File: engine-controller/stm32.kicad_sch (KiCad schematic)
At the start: 11 parts, among them IC201 STM32F103RBT6, J201 Conn_ARM_JTAG_SWD_20

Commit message: inital TCs
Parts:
- added C207, C208: 30p, Capacitor_SMD:C_0402_1005Metric, symbol Device:C_Small
- added Y201: 8MHz, Crystal:Crystal_SMD_5032-2Pin_5.0x3.2mm, symbol Device:Crystal_Small
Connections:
- net GND: now also C207.2, C208.2
- net SPI1_NSS: now reaches IC201.20 (PA4)
- net SPI1_SCK: now reaches IC201.21 (PA5)
- net SPI1_MISO: now reaches IC201.22 (PA6)
- net SPI1_MOSI: now reaches IC201.23 (PA7)
- net PC6: now reaches IC201.37 (PC6)
- net PC7: now reaches IC201.38 (PC7)
- net PC8: now reaches IC201.39 (PC8)
- net PC9: now reaches IC201.40 (PC9)
- net PA8: now reaches IC201.41 (PA8)
- net PA9: now reaches IC201.42 (PA9)
- net PA10: now reaches IC201.43 (PA10)
- net PA11: now reaches IC201.44 (PA11)
- net PA12: now reaches IC201.45 (PA12)
- net at IC201.5 (OSC_IN): now also C207.1, Y201.1
- net PB5: now reaches IC201.57 (PB5)
- net PB6: now reaches IC201.58 (PB6)
- net PB7: now reaches IC201.59 (PB7)
- net at IC201.6 (OSC_OUT): now also C208.1, Y201.2
- net PB8: now reaches IC201.61 (PB8)
- net PB9: now reaches IC201.62 (PB9)
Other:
- note added: "CL = 2 * (Cload - Cstray)"

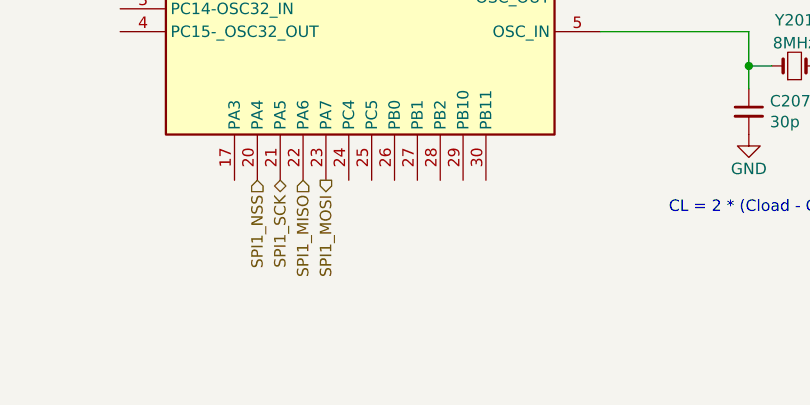
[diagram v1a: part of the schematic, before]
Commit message: added 4-20mA sense circuit
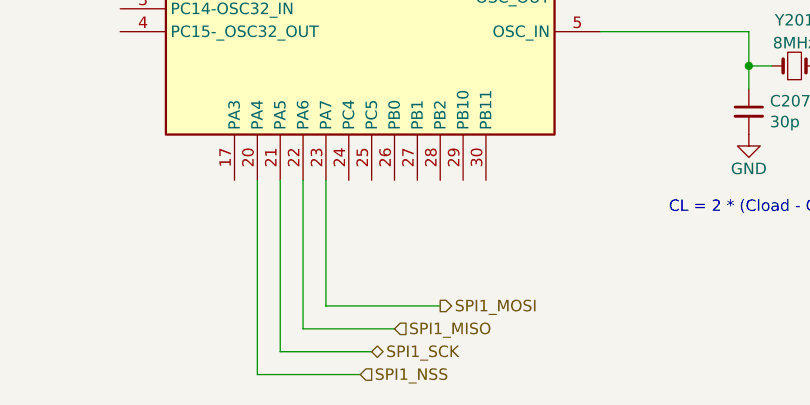
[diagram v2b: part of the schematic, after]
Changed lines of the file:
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@@
   (no_connect (at 71.12 68.58))
   (no_connect (at 71.12 83.82))
+  (wire (pts (xy 199.39 149.86) (xy 199.39 135.89))
+    (stroke (width 0) (type default))
+  )
   (wire (pts (xy 204.47 36.83) (xy 204.47 39.37))
     (stroke (width 0) (type default))
@@
     (stroke (width 0) (type default))
   )
+  (wire (pts (xy 203.2 157.48) (xy 191.77 157.48))
+    (stroke (width 0) (type default))
+  )
+  (wire (pts (xy 194.31 154.94) (xy 194.31 135.89))
+    (stroke (width 0) (type default))
+  )
   (wire (pts (xy 232.41 73.66) (xy 229.87 73.66))
     (stroke (width 0) (type default))
@@
     (stroke (width 0) (type default))
   )
+  (wire (pts (xy 196.85 152.4) (xy 196.85 135.89))
+    (stroke (width 0) (type default))
+  )
   (wire (pts (xy 201.93 33.02) (xy 201.93 39.37))
     (stroke (width 0) (type default))
@@
     (stroke (width 0) (type default))
   )
+  (wire (pts (xy 207.01 152.4) (xy 196.85 152.4))
+    (stroke (width 0) (type default))
+  )
   (wire (pts (xy 148.59 82.55) (xy 148.59 85.09))
     (stroke (width 0) (type default))
@@
     (stroke (width 0) (type default))
   )
+  (wire (pts (xy 204.47 154.94) (xy 194.31 154.94))
+    (stroke (width 0) (type default))
+  )
   (wire (pts (xy 229.87 63.5) (xy 254 63.5))
     (stroke (width 0) (type default))
@@
     (stroke (width 0) (type default))
   )
+  (wire (pts (xy 212.09 149.86) (xy 199.39 149.86))
+    (stroke (width 0) (type default))
+  )
   (wire (pts (xy 246.38 123.19) (xy 248.92 123.19))
     (stroke (width 0) (type default))
@@
   )
   (wire (pts (xy 114.3 53.34) (xy 124.46 53.34))
+    (stroke (width 0) (type default))
+  )
+  (wire (pts (xy 191.77 157.48) (xy 191.77 135.89))
     (stroke (width 0) (type default))
   )
@@
     (effects (font (size 1.27 1.27)) (justify left))
   )
-  (hierarchical_label "SPI1_SCK" (shape bidirectional) (at 194.31 135.89 270) (fields_autoplaced)
-    (effects (font (size 1.27 1.27)) (justify right))
+  (hierarchical_label "SPI1_SCK" (shape bidirectional) (at 204.47 154.94 0) (fields_autoplaced)
+    (effects (font (size 1.27 1.27)) (justify left))
   )
   (hierarchical_label "PC7" (shape output) (at 229.87 93.98 0) (fields_autoplaced)
@@
     (effects (font (size 1.27 1.27)) (justify left))
   )
-  (hierarchical_label "SPI1_MISO" (shape input) (at 196.85 135.89 270) (fields_autoplaced)
-    (effects (font (size 1.27 1.27)) (justify right))
+  (hierarchical_label "SPI1_MISO" (shape input) (at 207.01 152.4 0) (fields_autoplaced)
+    (effects (font (size 1.27 1.27)) (justify left))
   )
   (hierarchical_label "PA8" (shape output) (at 229.87 86.36 0) (fields_autoplaced)
@@
     (effects (font (size 1.27 1.27)) (justify left))
   )
-  (hierarchical_label "SPI1_MOSI" (shape output) (at 199.39 135.89 270) (fields_autoplaced)
-    (effects (font (size 1.27 1.27)) (justify right))
+  (hierarchical_label "SPI1_MOSI" (shape output) (at 212.09 149.86 0) (fields_autoplaced)
+    (effects (font (size 1.27 1.27)) (justify left))
   )
   (hierarchical_label "PB15" (shape output) (at 229.87 99.06 0) (fields_autoplaced)
     (effects (font (size 1.27 1.27)) (justify left))
   )
-  (hierarchical_label "SPI1_NSS" (shape input) (at 191.77 135.89 270) (fields_autoplaced)
-    (effects (font (size 1.27 1.27)) (justify right))
+  (hierarchical_label "SPI1_NSS" (shape input) (at 203.2 157.48 0) (fields_autoplaced)
+    (effects (font (size 1.27 1.27)) (justify left))
   )
   (hierarchical_label "PA9" (shape output) (at 229.87 83.82 0) (fields_autoplaced)

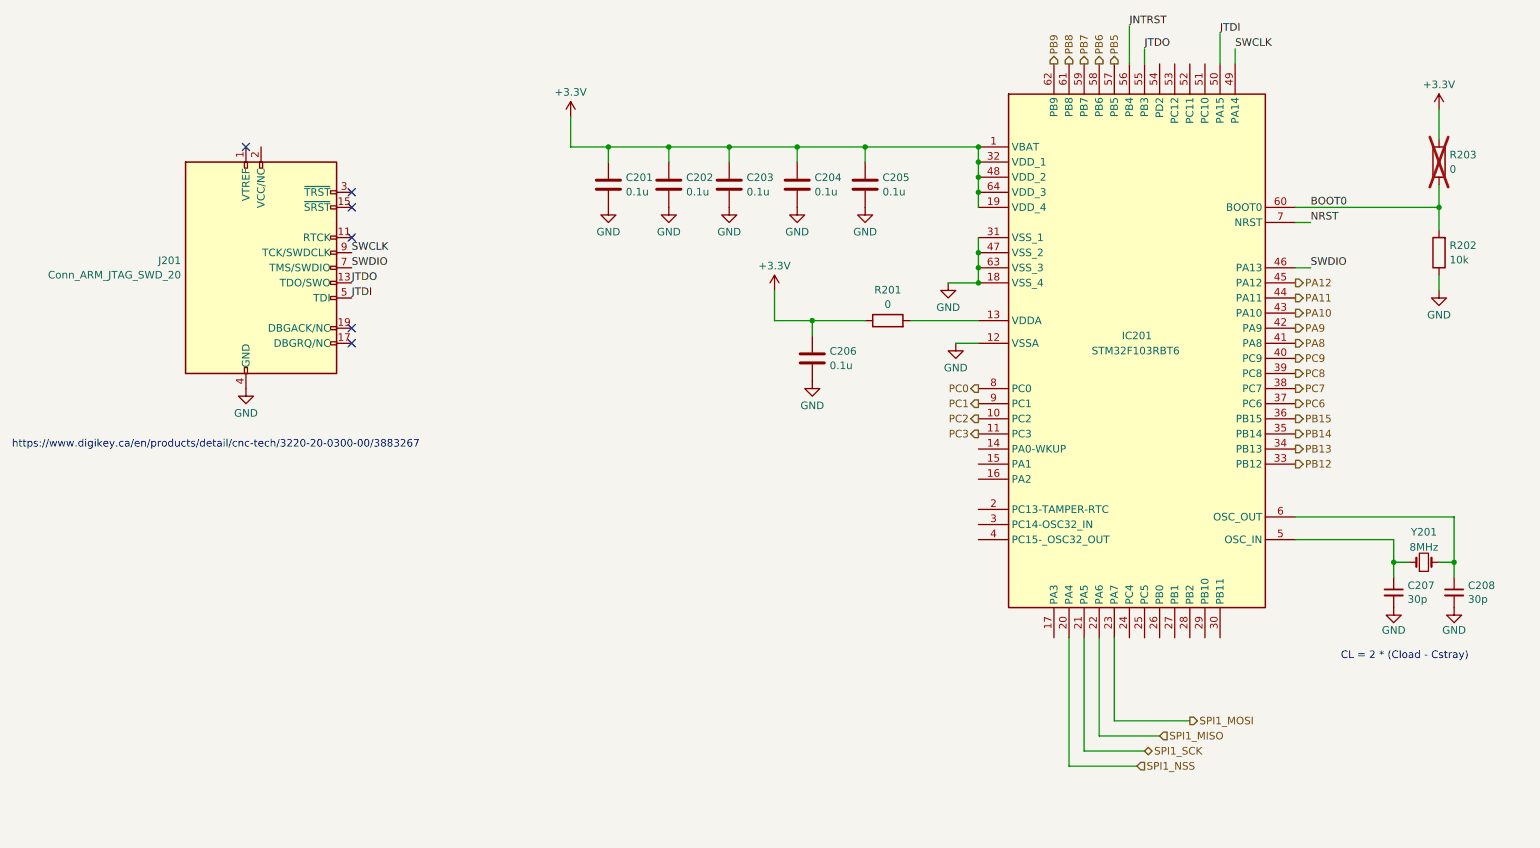
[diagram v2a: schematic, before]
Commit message: added switches
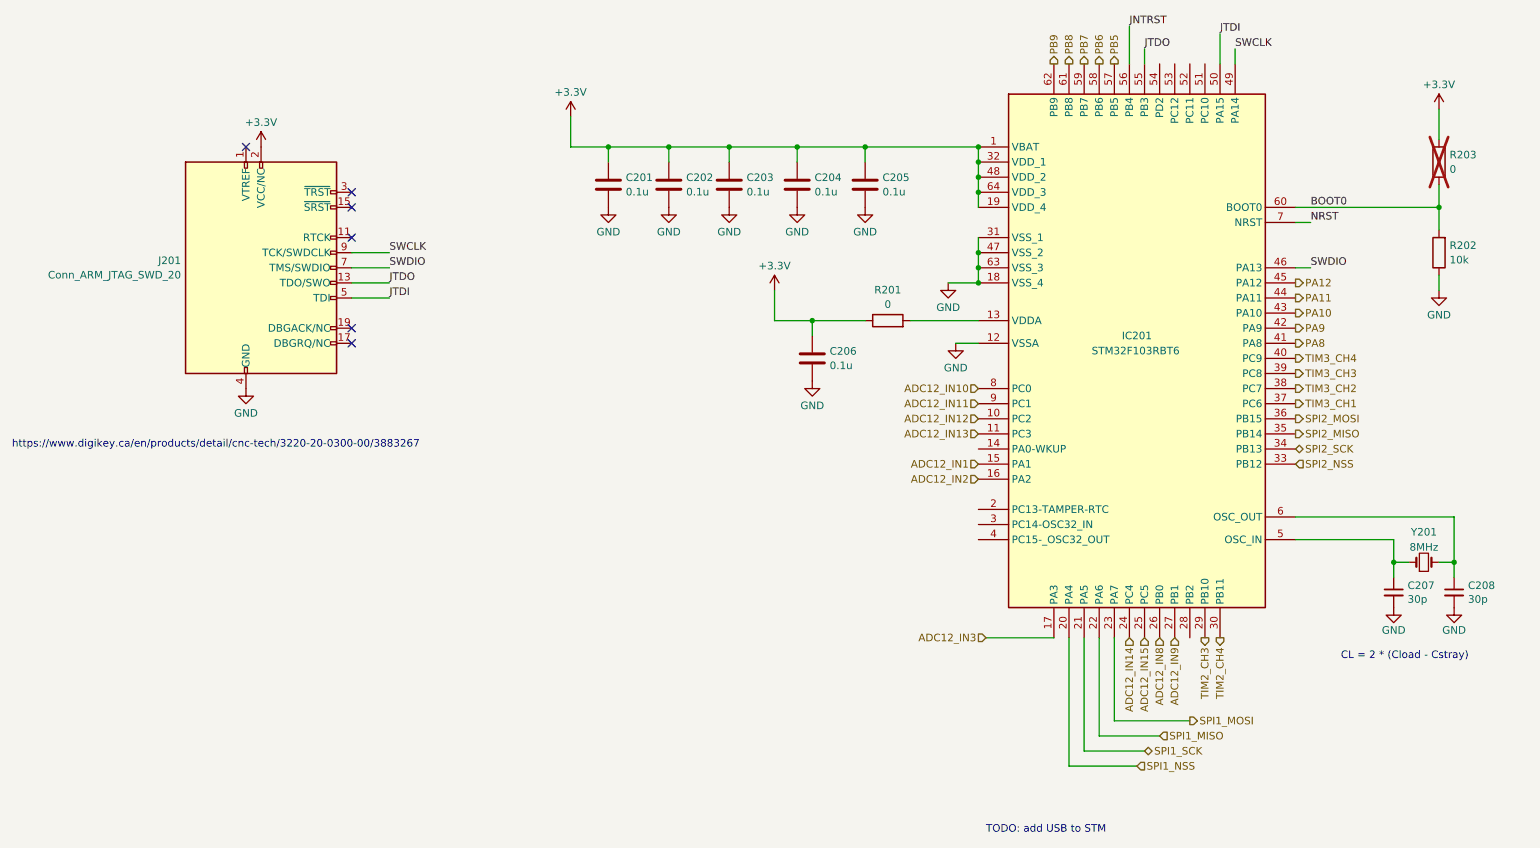
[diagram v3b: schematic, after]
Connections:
- net +3.3V: now also J201.2 (VCC/NC)
- net ADC12_IN1: now reaches IC201.15 (PA1)
- net ADC12_IN2: now reaches IC201.16 (PA2)
- net ADC12_IN3: now reaches IC201.17 (PA3)
- net ADC12_IN14: now reaches IC201.24 (PC4)
- net ADC12_IN15: now reaches IC201.25 (PC5)
- net ADC12_IN8: now reaches IC201.26 (PB0)
- net ADC12_IN9: now reaches IC201.27 (PB1)
- net TIM2_CH3: now reaches IC201.29 (PB10)
- net TIM2_CH4: now reaches IC201.30 (PB11)
- net PB12 renamed SPI2_NSS
- net PB13 renamed SPI2_SCK
- net PB14 renamed SPI2_MISO
- net PB15 renamed SPI2_MOSI
- net PC0 renamed ADC12_IN10
- net PC1 renamed ADC12_IN11
- net PC2 renamed ADC12_IN12
- net PC3 renamed ADC12_IN13
- net PC6 renamed TIM3_CH1
- net PC7 renamed TIM3_CH2
- net PC8 renamed TIM3_CH3
- net PC9 renamed TIM3_CH4
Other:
- note added: "TODO: add USB to STM"
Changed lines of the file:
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@@
+    (stroke (width 0) (type default))
+  )
+  (wire (pts (xy 77.47 78.74) (xy 71.12 78.74))
     (stroke (width 0) (type default))
   )
@@
     (stroke (width 0) (type default))
   )
+  (wire (pts (xy 77.47 71.12) (xy 71.12 71.12))
+    (stroke (width 0) (type default))
+  )
   (wire (pts (xy 232.41 66.04) (xy 229.87 66.04))
     (stroke (width 0) (type default))
@@
     (stroke (width 0) (type default))
   )
+  (wire (pts (xy 77.47 73.66) (xy 71.12 73.66))
+    (stroke (width 0) (type default))
+  )
   (wire (pts (xy 114.3 53.34) (xy 114.3 55.88))
     (stroke (width 0) (type default))
   )
+  (wire (pts (xy 77.47 76.2) (xy 71.12 76.2))
+    (stroke (width 0) (type default))
+  )
   (wire (pts (xy 172.72 86.36) (xy 176.53 86.36))
     (stroke (width 0) (type default))
@@
   )
   (wire (pts (xy 191.77 157.48) (xy 191.77 135.89))
+    (stroke (width 0) (type default))
+  )
+  (wire (pts (xy 177.8 135.89) (xy 189.23 135.89))
     (stroke (width 0) (type default))
   )
@@
     (effects (font (size 1.27 1.27)) (justify left bottom))
   )
+  (text "TODO: add USB to STM" (at 177.8 168.91 0)
+    (effects (font (size 1.27 1.27)) (justify left bottom))
+  )
   (label "BOOT0" (at 232.41 63.5 0) (fields_autoplaced)
     (effects (font (size 1.27 1.27)) (justify left bottom))
   )
-  (label "JTDO" (at 71.12 76.2 0) (fields_autoplaced)
+  (label "JTDO" (at 77.47 76.2 0) (fields_autoplaced)
     (effects (font (size 1.27 1.27)) (justify left bottom))
   )
@@
     (effects (font (size 1.27 1.27)) (justify left bottom))
   )
-  (label "JTDI" (at 71.12 78.74 0) (fields_autoplaced)
-    (effects (font (size 1.27 1.27)) (justify left bottom))
-  )
-  (label "SWCLK" (at 71.12 71.12 0) (fields_autoplaced)
-    (effects (font (size 1.27 1.27)) (justify left bottom))
-  )
-  (label "SWDIO" (at 71.12 73.66 0) (fields_autoplaced)
+  (label "JTDI" (at 77.47 78.74 0) (fields_autoplaced)
+    (effects (font (size 1.27 1.27)) (justify left bottom))
+  )
+  (label "SWCLK" (at 77.47 71.12 0) (fields_autoplaced)
+    (effects (font (size 1.27 1.27)) (justify left bottom))
+  )
+  (label "SWDIO" (at 77.47 73.66 0) (fields_autoplaced)
     (effects (font (size 1.27 1.27)) (justify left bottom))
   )
@@
     (effects (font (size 1.27 1.27)) (justify left bottom))
   )
-  (hierarchical_label "PC8" (shape output) (at 229.87 91.44 0) (fields_autoplaced)
-    (effects (font (size 1.27 1.27)) (justify left))
-  )
-  (hierarchical_label "PC9" (shape output) (at 229.87 88.9 0) (fields_autoplaced)
+  (hierarchical_label "ADC12_IN1" (shape input) (at 176.53 106.68 180) (fields_autoplaced)
+    (effects (font (size 1.27 1.27)) (justify right))
+  )
+  (hierarchical_label "TIM3_CH3" (shape output) (at 229.87 91.44 0) (fields_autoplaced)
     (effects (font (size 1.27 1.27)) (justify left))
   )
@@
     (effects (font (size 1.27 1.27)) (justify left))
   )
-  (hierarchical_label "PC7" (shape output) (at 229.87 93.98 0) (fields_autoplaced)
-    (effects (font (size 1.27 1.27)) (justify left))
-  )
   (hierarchical_label "PB7" (shape output) (at 194.31 39.37 90) (fields_autoplaced)
     (effects (font (size 1.27 1.27)) (justify left))
@@
     (effects (font (size 1.27 1.27)) (justify left))
   )
+  (hierarchical_label "TIM3_CH4" (shape output) (at 229.87 88.9 0) (fields_autoplaced)
+    (effects (font (size 1.27 1.27)) (justify left))
+  )
+  (hierarchical_label "TIM2_CH3" (shape output) (at 214.63 135.89 270) (fields_autoplaced)
+    (effects (font (size 1.27 1.27)) (justify right))
+  )
   (hierarchical_label "PA12" (shape output) (at 229.87 76.2 0) (fields_autoplaced)
     (effects (font (size 1.27 1.27)) (justify left))
@@
     (effects (font (size 1.27 1.27)) (justify left))
   )
+  (hierarchical_label "ADC12_IN8" (shape input) (at 207.01 135.89 270) (fields_autoplaced)
+    (effects (font (size 1.27 1.27)) (justify right))
+  )
   (hierarchical_label "SPI1_MISO" (shape input) (at 207.01 152.4 0) (fields_autoplaced)
     (effects (font (size 1.27 1.27)) (justify left))
@@
     (effects (font (size 1.27 1.27)) (justify left))
   )
-  (hierarchical_label "PB13" (shape output) (at 229.87 104.14 0) (fields_autoplaced)
-    (effects (font (size 1.27 1.27)) (justify left))
-  )
-  (hierarchical_label "PC3" (shape output) (at 176.53 101.6 180) (fields_autoplaced)
-    (effects (font (size 1.27 1.27)) (justify right))
-  )
-  (hierarchical_label "PC0" (shape output) (at 176.53 93.98 180) (fields_autoplaced)
-    (effects (font (size 1.27 1.27)) (justify right))
-  )
-  (hierarchical_label "PC6" (shape output) (at 229.87 96.52 0) (fields_autoplaced)
-    (effects (font (size 1.27 1.27)) (justify left))
-  )
-  (hierarchical_label "PB12" (shape output) (at 229.87 106.68 0) (fields_autoplaced)
-    (effects (font (size 1.27 1.27)) (justify left))
-  )
-  (hierarchical_label "PB14" (shape output) (at 229.87 101.6 0) (fields_autoplaced)
+  (hierarchical_label "SPI2_SCK" (shape bidirectional) (at 229.87 104.14 0) (fields_autoplaced)
+    (effects (font (size 1.27 1.27)) (justify left))
+  )
+  (hierarchical_label "ADC12_IN3" (shape input) (at 177.8 135.89 180) (fields_autoplaced)
+    (effects (font (size 1.27 1.27)) (justify right))
+  )
+  (hierarchical_label "ADC12_IN13" (shape input) (at 176.53 101.6 180) (fields_autoplaced)
+    (effects (font (size 1.27 1.27)) (justify right))
+  )
+  (hierarchical_label "ADC12_IN10" (shape input) (at 176.53 93.98 180) (fields_autoplaced)
+    (effects (font (size 1.27 1.27)) (justify right))
+  )
+  (hierarchical_label "TIM3_CH1" (shape output) (at 229.87 96.52 0) (fields_autoplaced)
+    (effects (font (size 1.27 1.27)) (justify left))
+  )
+  (hierarchical_label "ADC12_IN2" (shape input) (at 176.53 109.22 180) (fields_autoplaced)
+    (effects (font (size 1.27 1.27)) (justify right))
+  )
+  (hierarchical_label "TIM2_CH4" (shape output) (at 217.17 135.89 270) (fields_autoplaced)
+    (effects (font (size 1.27 1.27)) (justify right))
+  )
+  (hierarchical_label "SPI2_NSS" (shape input) (at 229.87 106.68 0) (fields_autoplaced)
+    (effects (font (size 1.27 1.27)) (justify left))
+  )
+  (hierarchical_label "SPI2_MISO" (shape output) (at 229.87 101.6 0) (fields_autoplaced)
+    (effects (font (size 1.27 1.27)) (justify left))
+  )
+  (hierarchical_label "TIM3_CH2" (shape output) (at 229.87 93.98 0) (fields_autoplaced)
     (effects (font (size 1.27 1.27)) (justify left))
   )
@@
     (effects (font (size 1.27 1.27)) (justify left))
   )
+  (hierarchical_label "ADC12_IN9" (shape input) (at 209.55 135.89 270) (fields_autoplaced)
+    (effects (font (size 1.27 1.27)) (justify right))
+  )
+  (hierarchical_label "ADC12_IN15" (shape input) (at 204.47 135.89 270) (fields_autoplaced)
+    (effects (font (size 1.27 1.27)) (justify right))
+  )
   (hierarchical_label "PA11" (shape output) (at 229.87 78.74 0) (fields_autoplaced)
     (effects (font (size 1.27 1.27)) (justify left))
   )
+  (hierarchical_label "ADC12_IN14" (shape input) (at 201.93 135.89 270) (fields_autoplaced)
+    (effects (font (size 1.27 1.27)) (justify right))
+  )
   (hierarchical_label "PB8" (shape output) (at 191.77 39.37 90) (fields_autoplaced)
     (effects (font (size 1.27 1.27)) (justify left))
@@
     (effects (font (size 1.27 1.27)) (justify left))
   )
-  (hierarchical_label "PB15" (shape output) (at 229.87 99.06 0) (fields_autoplaced)
+  (hierarchical_label "SPI2_MOSI" (shape output) (at 229.87 99.06 0) (fields_autoplaced)
     (effects (font (size 1.27 1.27)) (justify left))
   )
@@
     (effects (font (size 1.27 1.27)) (justify left))
   )
-  (hierarchical_label "PC1" (shape output) (at 176.53 96.52 180) (fields_autoplaced)
+  (hierarchical_label "ADC12_IN11" (shape input) (at 176.53 96.52 180) (fields_autoplaced)
     (effects (font (size 1.27 1.27)) (justify right))
   )
@@
     (effects (font (size 1.27 1.27)) (justify left))
   )
-  (hierarchical_label "PC2" (shape output) (at 176.53 99.06 180) (fields_autoplaced)
+  (hierarchical_label "ADC12_IN12" (shape input) (at 176.53 99.06 180) (fields_autoplaced)
     (effects (font (size 1.27 1.27)) (justify right))
   )
@@
         )
       )
+    )
+  )
+  (symbol (lib_id "power:+3.3V") (at 55.88 53.34 0) (unit 1)
+    (in_bom yes) (on_board yes) (dnp no) (fields_autoplaced)
+    (property "Reference" "#PWR01" (at 55.88 57.15 0)
+      (effects (font (size 1.27 1.27)) hide)
+    )
+    (property "Value" "+3.3V" (at 55.88 49.2069 0)
+      (effects (font (size 1.27 1.27)))
+    )
+    (property "Footprint" "" (at 55.88 53.34 0)
+      (effects (font (size 1.27 1.27)) hide)
+    )
+    (property "Datasheet" "" (at 55.88 53.34 0)
+      (effects (font (size 1.27 1.27)) hide)
+    )
+    (pin "1")
+    (instances
+      (project "engine-controller"
+        (path "/c646003c-e1a1-4f96-833a-f6a146234064/4fb5d043-5efd-4b64-9ebf-9dabbf04a320"
+          (reference "#PWR01") (unit 1)
+        )
+      )

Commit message: initial layout
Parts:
- IC201: footprint QFP50P1200X1200X160-64N -> SamacSys_Parts:QFP50P1200X1200X160-64N
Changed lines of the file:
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@@
       (effects (font (size 1.27 1.27)) (justify left))
     )
-    (property "Footprint" "QFP50P1200X1200X160-64N" (at 226.06 153.34 0)
+    (property "Footprint" "SamacSys_Parts:QFP50P1200X1200X160-64N" (at 226.06 153.34 0)
       (effects (font (size 1.27 1.27)) (justify left top) hide)
     )
